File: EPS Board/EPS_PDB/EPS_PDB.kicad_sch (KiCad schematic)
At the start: 16 parts, among them J1 USB_B_Micro, J2 Conn_01x04_Pin, J3 Conn_02x26_Odd_Even, J4 Conn_02x26_Odd_Even, U1 AMS1117-3.3

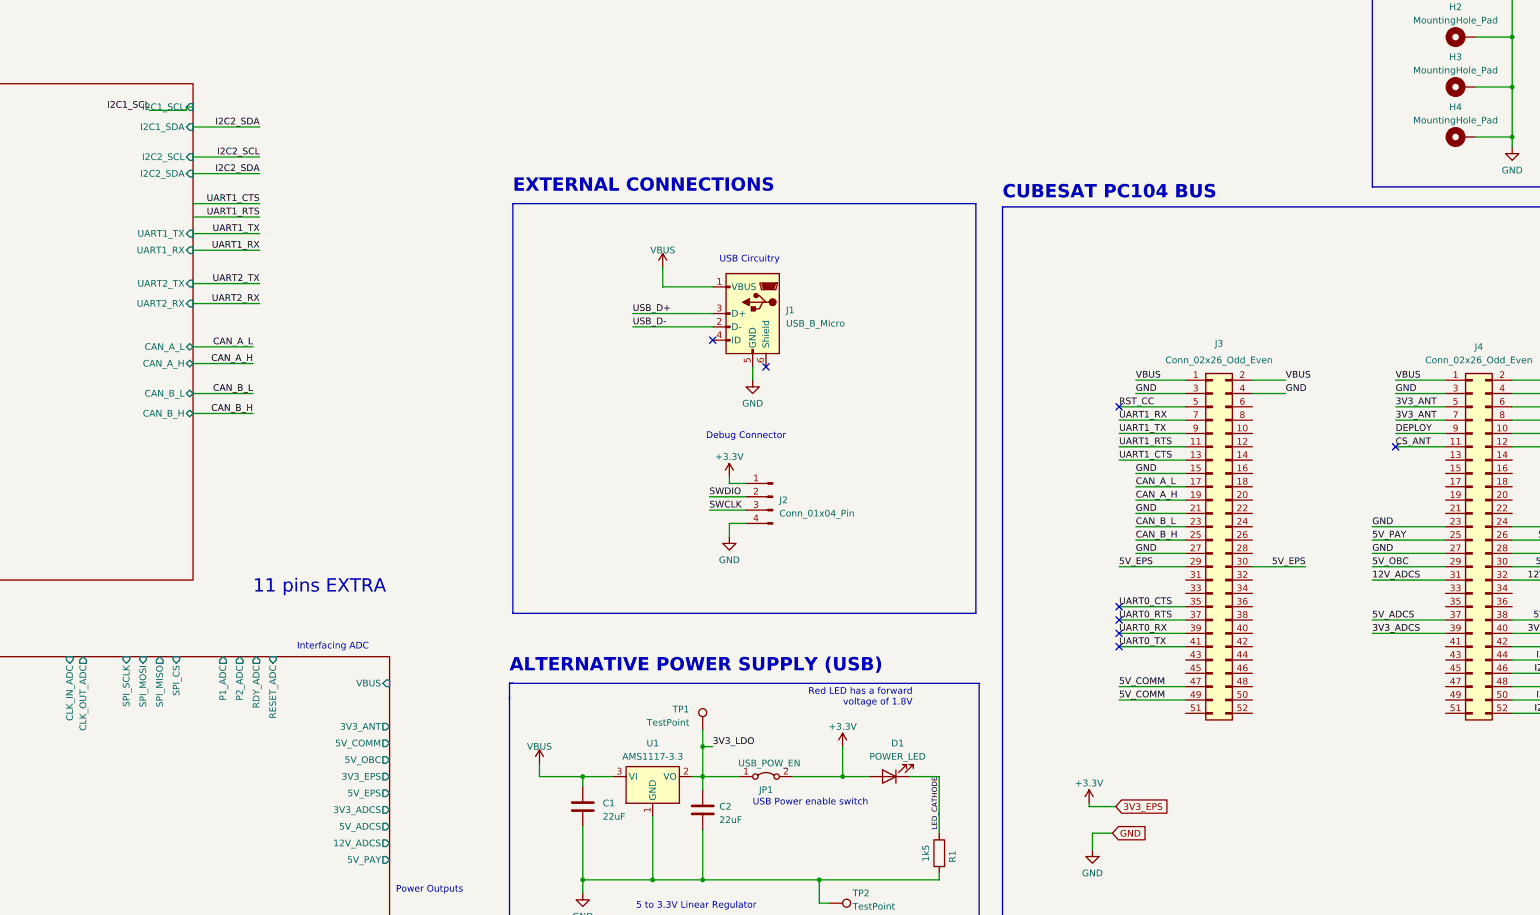
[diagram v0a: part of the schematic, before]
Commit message: Added Heartbeat GPIOs from ADCS and OBC
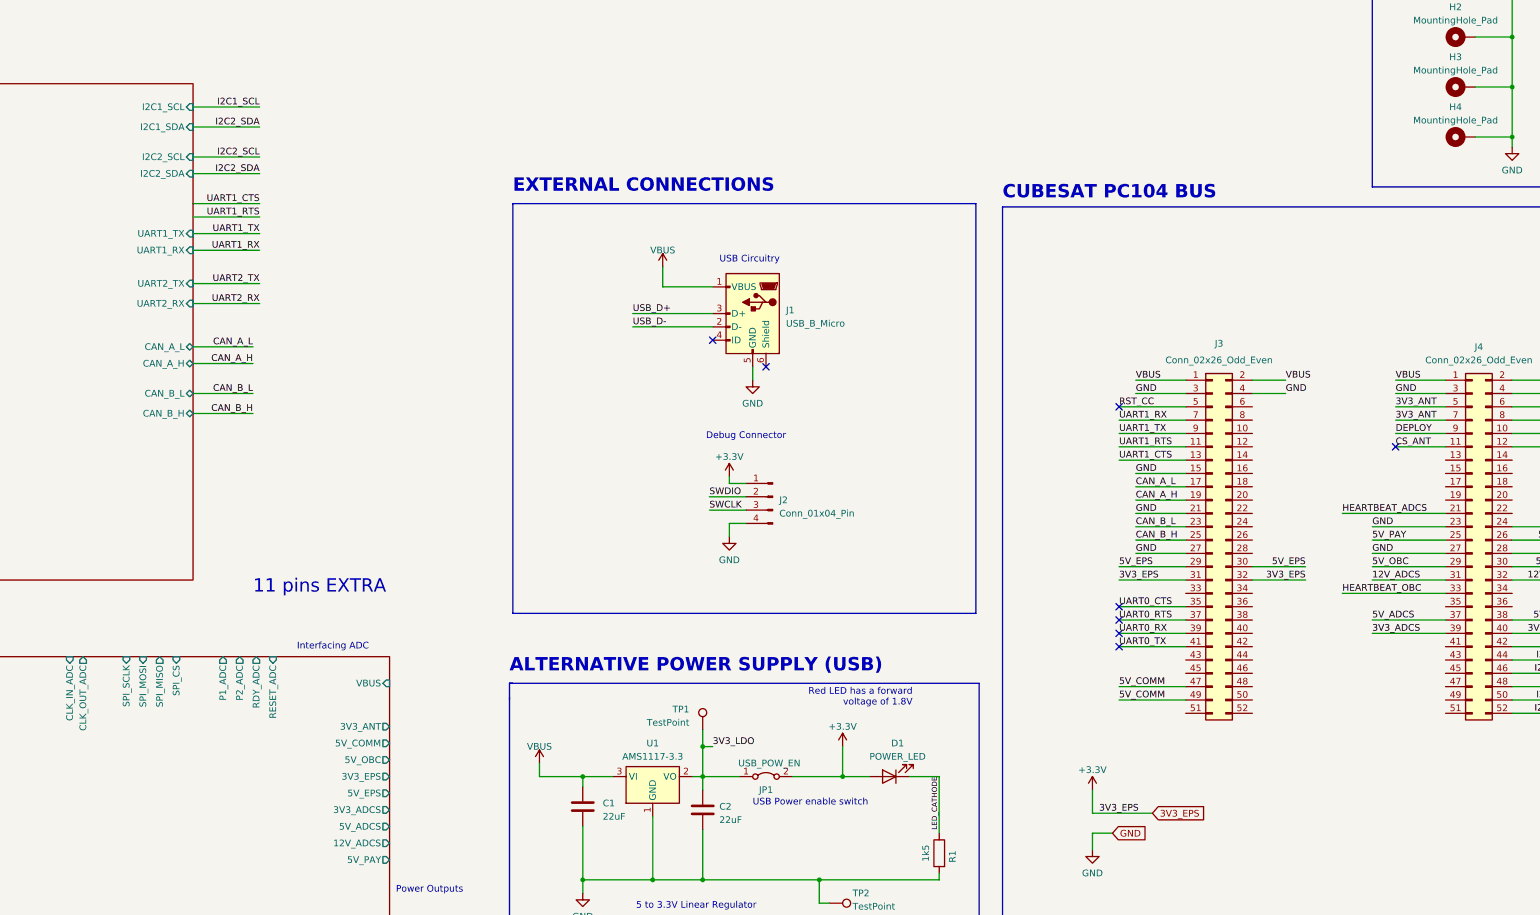
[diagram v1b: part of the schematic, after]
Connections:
- net +3.3V: now also J3.31 (Pin_31), J3.32 (Pin_32)
- net HEARTBEAT_ADCS: now reaches J4.21 (Pin_21)
- net HEARTBEAT_OBC: now reaches J4.33 (Pin_33)
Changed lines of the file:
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@@
 	(wire
 		(pts
-			(xy 116.205 73.025) (xy 109.22 73.025)
-		)
-		(stroke
-			(width 0)
-			(type default)
-		)
-	)
-	(wire
-		(pts
 			(xy 342.265 162.56) (xy 356.235 162.56)
 		)
@@
 	(wire
 		(pts
+			(xy 117.475 72.39) (xy 130.175 72.39)
+		)
+		(stroke
+			(width 0)
+			(type default)
+		)
+	)
+	(wire
+		(pts
 			(xy 215.9 149.225) (xy 222.885 149.225)
 		)
@@
 	(wire
 		(pts
-			(xy 288.29 205.74) (xy 293.37 205.74)
+			(xy 288.925 207.01) (xy 300.355 207.01)
 		)
 		(stroke
@@
 	(wire
 		(pts
-			(xy 288.29 205.105) (xy 288.29 205.74)
+			(xy 288.925 202.565) (xy 288.925 207.01)
 		)
 		(stroke
@@
 	(wire
 		(pts
+			(xy 336.55 165.1) (xy 356.235 165.1)
+		)
+		(stroke
+			(width 0)
+			(type default)
+		)
+	)
+	(wire
+		(pts
 			(xy 214.63 191.135) (xy 214.63 194.31)
 		)
@@
 	(wire
 		(pts
-			(xy 297.18 127) (xy 306.705 127)
+			(xy 336.55 149.86) (xy 356.235 149.86)
 		)
 		(stroke
@@
 	(wire
 		(pts
-			(xy 294.005 132.08) (xy 306.705 132.08)
+			(xy 297.18 127) (xy 306.705 127)
 		)
 		(stroke
@@
 	(wire
 		(pts
-			(xy 116.205 72.39) (xy 116.205 73.025)
+			(xy 294.005 132.08) (xy 306.705 132.08)
 		)
 		(stroke
@@
 	(wire
 		(pts
+			(xy 294.005 162.56) (xy 306.705 162.56)
+		)
+		(stroke
+			(width 0)
+			(type default)
+		)
+	)
+	(wire
+		(pts
 			(xy 205.105 207.645) (xy 205.105 219.71)
 		)
@@
 	(wire
 		(pts
-			(xy 117.475 72.39) (xy 116.205 72.39)
-		)
-		(stroke
-			(width 0)
-			(type default)
-		)
-	)
-	(wire
-		(pts
 			(xy 368.935 177.8) (xy 381.635 177.8)
 		)
@@
 	(wire
 		(pts
+			(xy 319.405 162.56) (xy 329.565 162.56)
+		)
+		(stroke
+			(width 0)
+			(type default)
+		)
+	)
+	(wire
+		(pts
 			(xy 216.535 194.31) (xy 214.63 194.31)
 		)
@@
 		)
 	)
+	(label "HEARTBEAT_OBC"
+		(at 336.55 165.1 0)
+		(fields_autoplaced yes)
+		(effects
+			(font
+				(size 1.27 1.27)
+			)
+			(justify left bottom)
+		)
+	)
 	(label "VBUS"
 		(at 375.285 124.46 0)
@@
 		)
 	)
+	(label "HEARTBEAT_ADCS"
+		(at 336.55 149.86 0)
+		(fields_autoplaced yes)
+		(effects
+			(font
+				(size 1.27 1.27)
+			)
+			(justify left bottom)
+		)
+	)
 	(label "SWCLK"
 		(at 215.9 149.225 0)
@@
 		)
 	)
+	(label "3V3_EPS"
+		(at 290.195 207.01 0)
+		(fields_autoplaced yes)
+		(effects
+			(font
+				(size 1.27 1.27)
+			)
+			(justify left bottom)
+		)
+	)
 	(label "VBUS"
 		(at 297.18 124.46 0)
@@
 		)
 	)
+	(label "3V3_EPS"
+		(at 294.005 162.56 0)
+		(fields_autoplaced yes)
+		(effects
+			(font
+				(size 1.27 1.27)
+			)
+			(justify left bottom)
+		)
+	)
 	(label "UART1_TX"
 		(at 294.005 134.62 0)
@@
 	)
 	(label "I2C1_SCL"
-		(at 109.22 73.025 180)
+		(at 130.175 72.39 180)
 		(fields_autoplaced yes)
 		(effects
@@
 		)
 	)
+	(label "3V3_EPS"
+		(at 329.565 162.56 180)
+		(fields_autoplaced yes)
+		(effects
+			(font
+				(size 1.27 1.27)
+			)
+			(justify right bottom)
+		)
+	)
 	(label "GND"
 		(at 325.755 127 0)
@@
 	(global_label "3V3_EPS"
 		(shape input)
-		(at 293.37 205.74 0)
+		(at 300.355 207.01 0)
 		(fields_autoplaced yes)
 		(effects
@@
 		)
 		(property "Intersheetrefs" "${INTERSHEET_REFS}"
-			(at 304.3795 205.74 0)
+			(at 311.3645 207.01 0)
 			(effects
 				(font
@@
 	(symbol
 		(lib_id "power:+3.3V")
-		(at 288.29 205.105 0)
+		(at 288.925 202.565 0)
 		(unit 1)
 		(exclude_from_sim no)
@@
 		(fields_autoplaced yes)
 		(property "Reference" "#PWR08"
-			(at 288.29 208.915 0)
+			(at 288.925 206.375 0)
 			(effects
 				(font
@@
 		)
 		(property "Value" "+3.3V"
-			(at 288.29 201.295 0)
+			(at 288.925 198.755 0)
 			(effects
 				(font
@@
 		)
 		(property "Footprint" ""
-			(at 288.29 205.105 0)
+			(at 288.925 202.565 0)
 			(effects
 				(font
@@
 		)
 		(property "Datasheet" ""
-			(at 288.29 205.105 0)
+			(at 288.925 202.565 0)
 			(effects
 				(font
@@
 		)
 		(property "Description" ""
-			(at 288.29 205.105 0)
+			(at 288.925 202.565 0)
 			(effects
 				(font

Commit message: Interfaced Control and PD&R unit
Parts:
- added JP4: Jumper_2_Bridged, symbol Jumper:Jumper_2_Bridged
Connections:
- net HEARTBEAT_OBC: now also J4.19 (Pin_19); no longer J4.33 (Pin_33)
- net VBUS: now also JP4.2 (B); no longer J3.1 (Pin_1), J3.2 (Pin_2), J4.1 (Pin_1), J4.2 (Pin_2)
- net 5V_EPS renamed +5V
- net DEPLOY renamed ANT_DEPLOY
- net DEPLOY_STATUS renamed ANT_DEPLOY_STATUS
- new net VBUS0: J3.1 (Pin_1), J3.2 (Pin_2), J4.1 (Pin_1), J4.2 (Pin_2), JP4.1 (A)
- no-connect marks 9 -> 53
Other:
- sheet EPS Control Unit ports: added ANT_DEPLOY, ANT_DEPLOY_STATUS, FLT_3V3_EPS, HEARTBEAT_ADCS, HEARTBEAT_OBC, P1_ADC, P2_ADC, RDY_ADC, RESET_ADC, SHDN_12V, SPI_CS, SPI_MISO, SPI_MOSI, SPI_SCLK, STATUS_3V3, STATUS_5V, UART1_CTS, UART1_RTS; removed 12V_SHDN, 3V3_STATUS, 5V_STATUS, UART2_RX, UART2_TX
- sheet EPS Power Distribution ports: added SHDN_12V, STATUS_3V3, STATUS_5V; removed 12V_SHDN, 3V3_STATUS, 5V_STATUS, CLK_IN_ADC, CLK_OUT_ADC
- note added: "ADCS"
- note added: "ANT"
- note added: "ANT_DEPLOY"
- note added: "COMM"
- note added: "COMM UART"
- note added: "CURRENT_MONITOR"
- note added: "EPS"
- note added: "EPS CAN COMMS"
- note added: "EPS CONTROL UNIT"
- note added: "EPS PDB Board uses 2 Voltage lines 1. 3V3_EPS 2. 5V_EPS"
- note added: "EPS POWER DISTRIBUTION AND REGULATION UNIT"
- note added: "HARSHIL SINGLA"
- note added: "HBT"
- note added: "I2C1"
- note added: "I2C2"
- note added: "Link to Electrical Pin Definitions Sheet"
- note added: "OBC"
- note added: "PAY"
- note added: "POWER SUPPLY"
- note added: "QAed BY:"
- note added: "REMOVE (ADD) BEFORE FLIGHT"
- note added: "SEPT 2024"
- note added: "SPI"
- note added: "Serial Wire Debug Connector"
- note added: "USB Connector"
- note added: "VOLTAGE_MONITOR"
- note removed: "11 pins EXTRA"
- note removed: "Debug Connector"
- note removed: "Power Outputs"
- note removed: "Reminder to use 1206 caps on 12V lines"
- note removed: "USB Circuitry"
- moved on the sheet: C1, C2, D1, H1, H2, H3, H4, J2, J3, J4, JP1, R1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

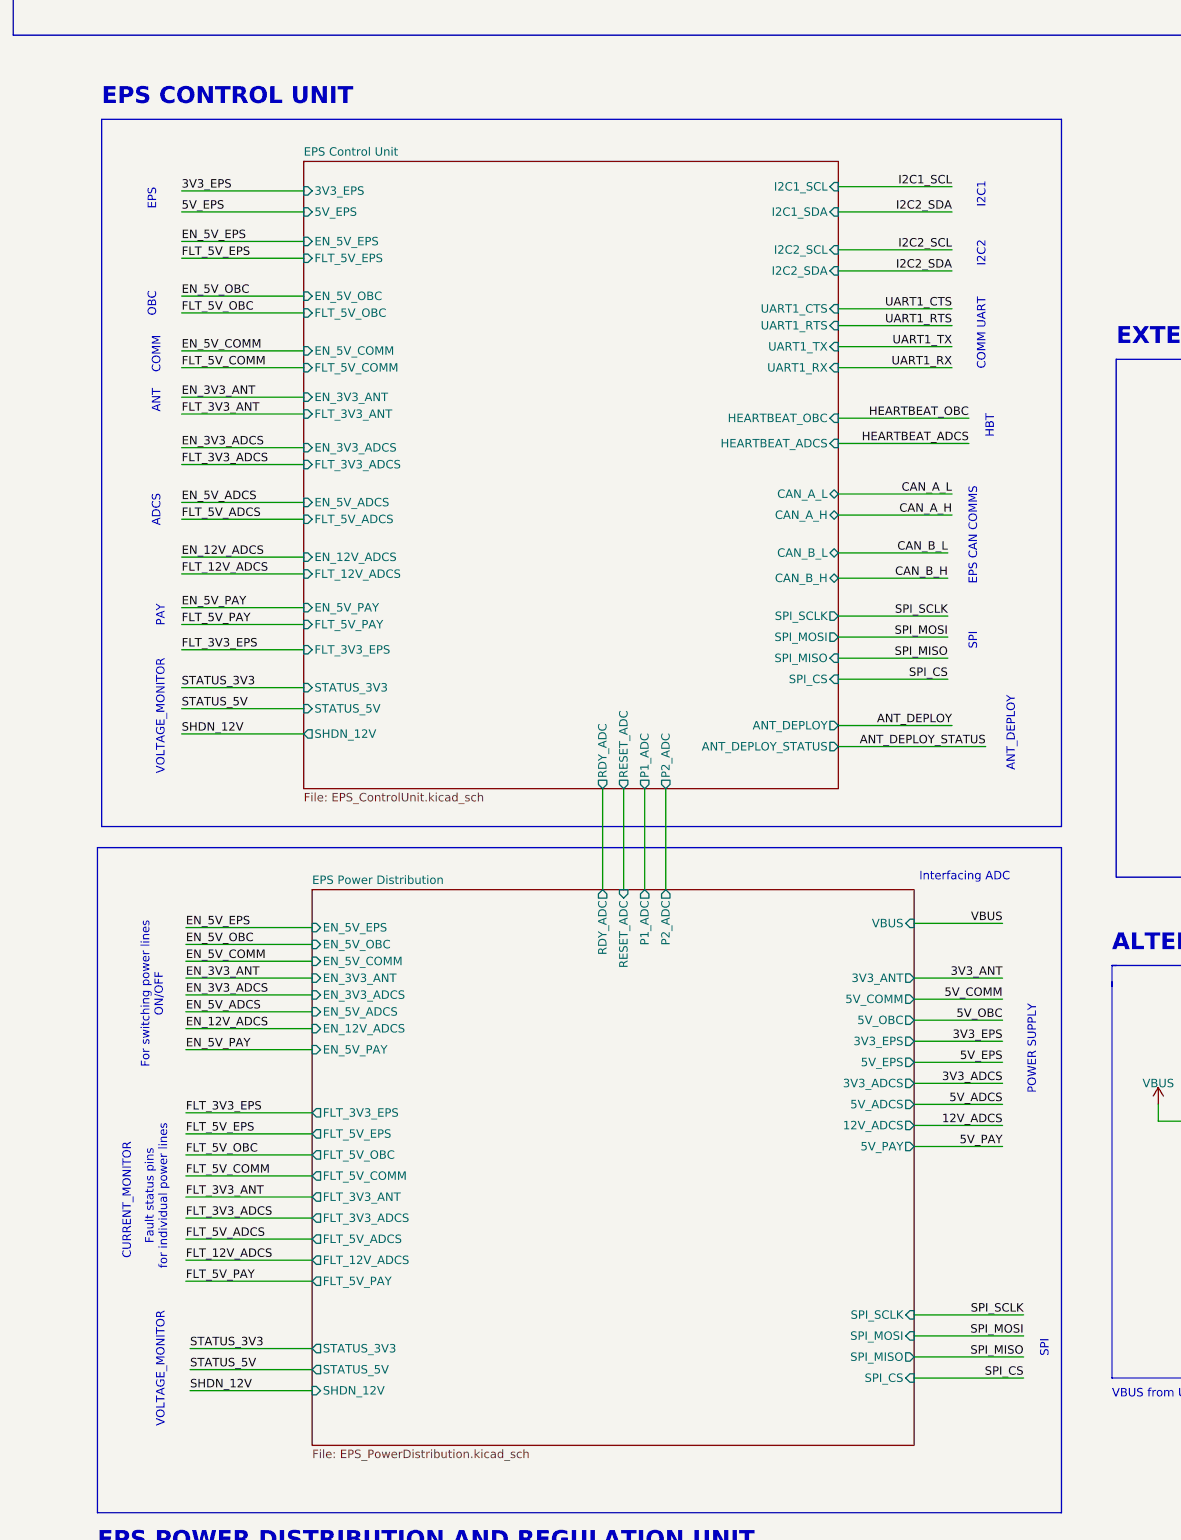
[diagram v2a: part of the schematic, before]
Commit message: Reference voltage ic, clock, ADC schematic done
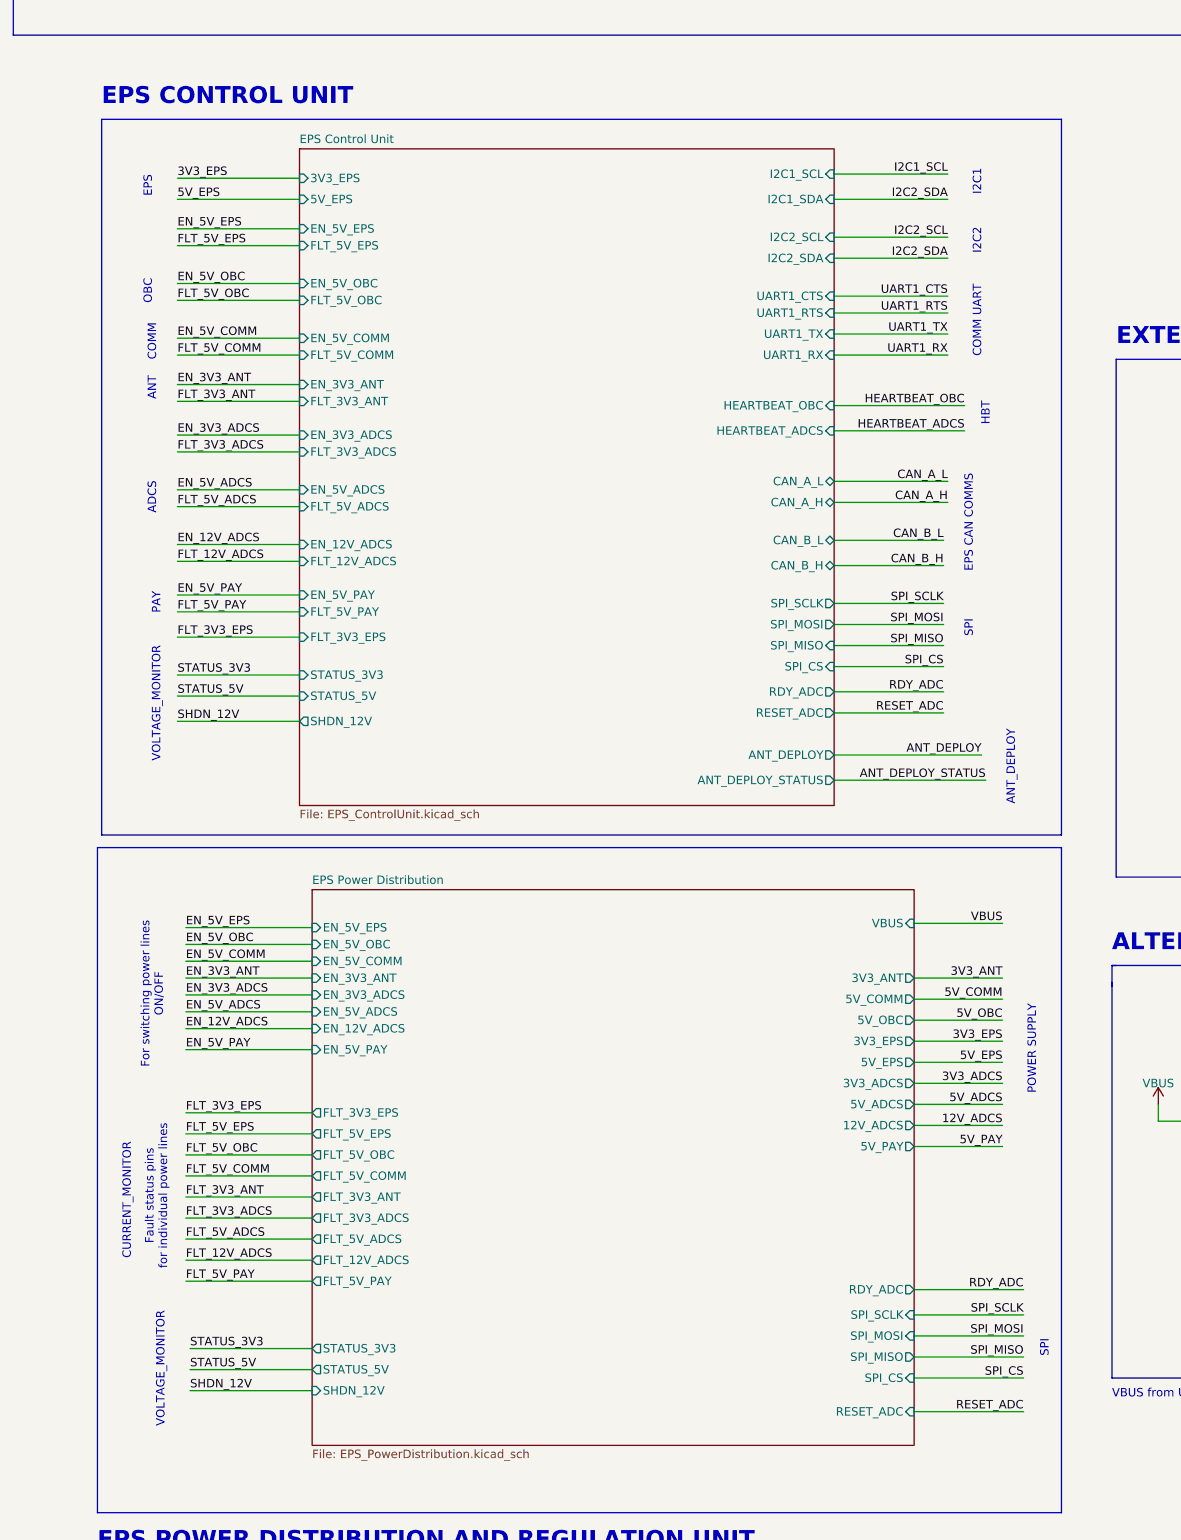
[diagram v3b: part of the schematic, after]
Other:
- sheet EPS Control Unit ports: added none; removed P1_ADC, P2_ADC
- sheet EPS Power Distribution ports: added none; removed P1_ADC, P2_ADC
- note removed: "Interfacing ADC"
